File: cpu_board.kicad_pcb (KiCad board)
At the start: 4 copper layers, 63 parts, among them J1 Conn_01x13, J10 Conn_02x12_Odd_Even, J11 Conn_02x12_Odd_Even, J12 Conn_02x12_Odd_Even, J13 Conn_02x12_Odd_Even, J14 Conn_02x12_Odd_Even, J15 Conn_02x12_Odd_Even, J2 Conn_02x05_Odd_Even, J3 Conn_02x12_Odd_Even, J4 Conn_01x13, J5 Conn_02x12_Odd_Even, J6 Conn_02x12_Odd_Even, J7 Conn_02x12_Odd_Even, J8 Conn_02x12_Odd_Even, J9 Conn_02x12_Odd_Even, U1 74HC191, U2 74HC191, U3 74HC191, U4 74HC245, U5 74HC245, U6 74HC02, U7 74HC08

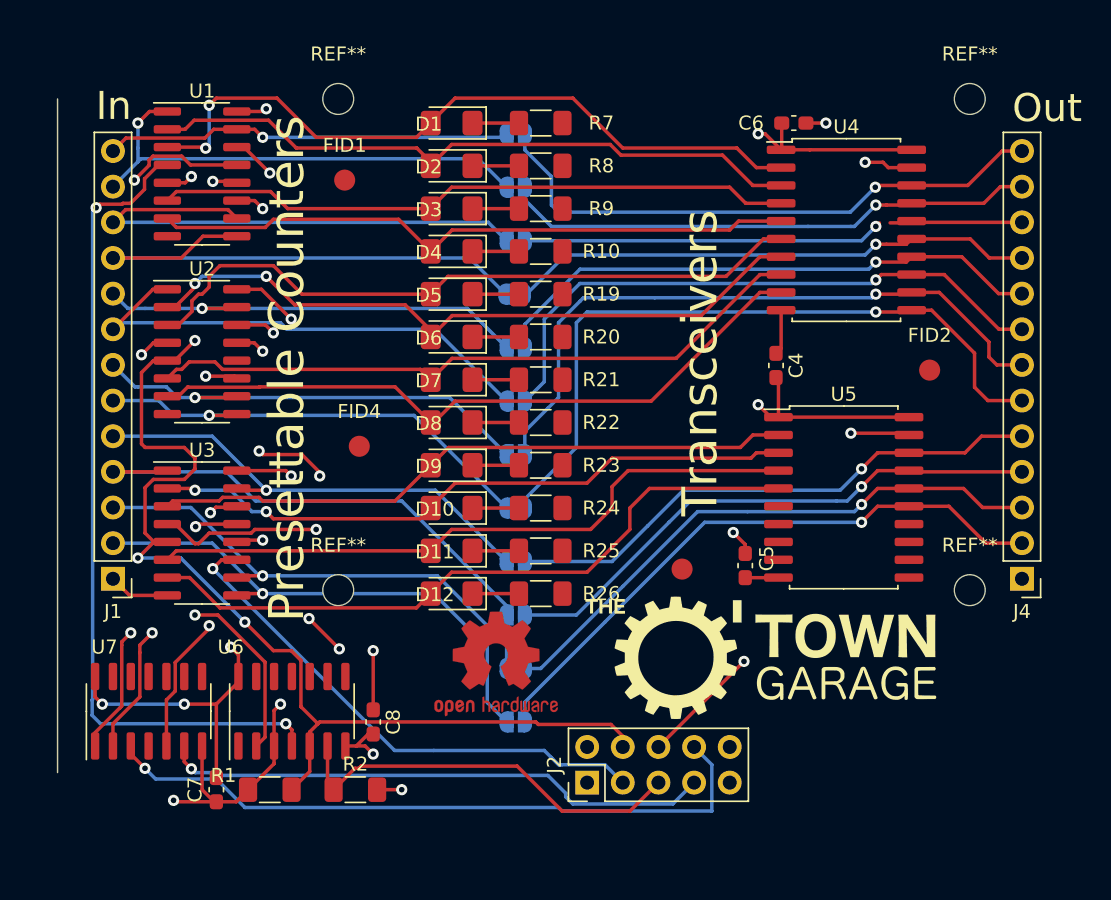
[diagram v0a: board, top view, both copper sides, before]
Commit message: Add edge cuts
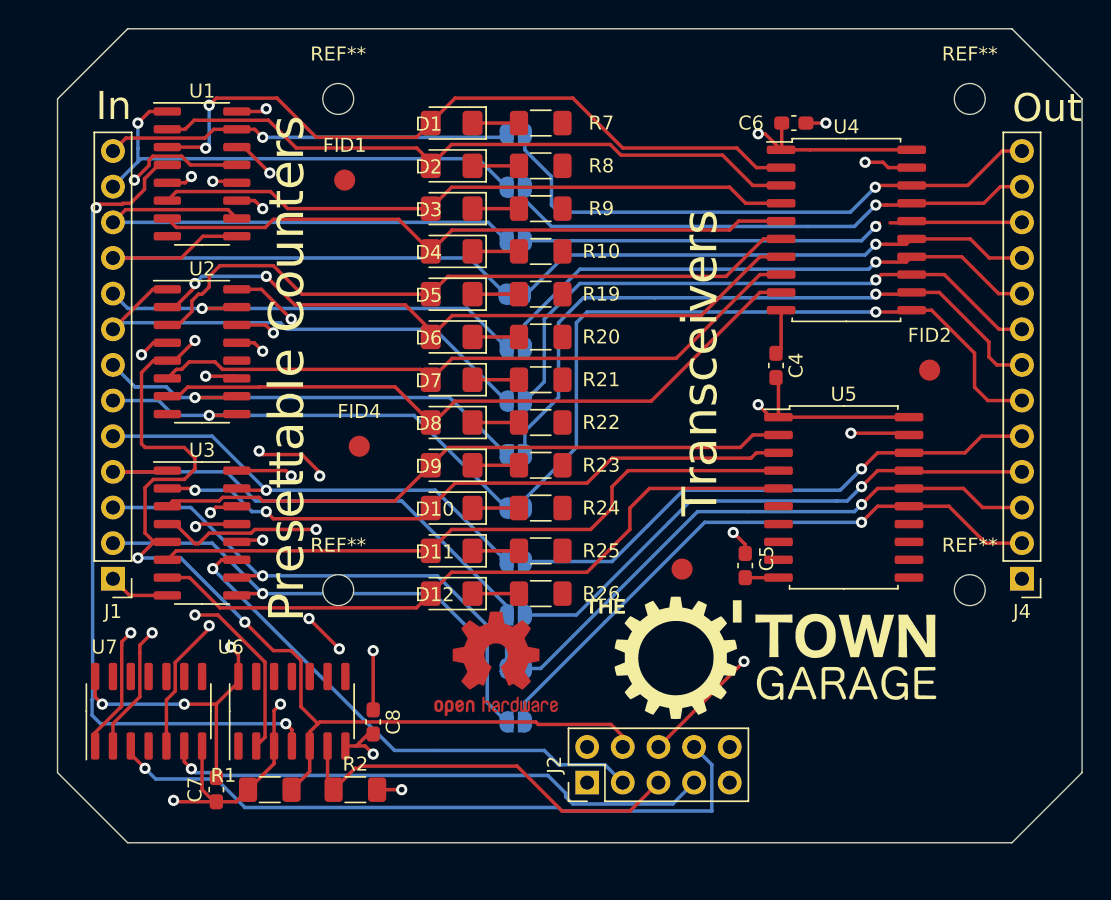
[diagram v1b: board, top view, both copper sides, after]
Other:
- board outline added: 73 x 58 mm
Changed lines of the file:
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@@
       ))
   )
+  (gr_line (start 123 103) (end 123 55) (layer "Edge.Cuts") (width 0.1))
+  (gr_line (start 118 50) (end 55 50) (layer "Edge.Cuts") (width 0.1))
+  (gr_line (start 123 55) (end 118 50) (layer "Edge.Cuts") (width 0.1))
+  (gr_line (start 118 108) (end 123 103) (layer "Edge.Cuts") (width 0.1))
+  (gr_line (start 55 50) (end 50 55) (layer "Edge.Cuts") (width 0.1))
   (gr_line (start 50 55) (end 50 103) (layer "Edge.Cuts") (width 0.1))
+  (gr_line (start 55 108) (end 118 108) (layer "Edge.Cuts") (width 0.1))
+  (gr_line (start 55 108) (end 50 103) (layer "Edge.Cuts") (width 0.1))
   (gr_text "Transceivers" (at 95.783 73.8134 90) (layer "F.SilkS")
     (effects (font (size 2.5 2.5) (thickness 0.4)))

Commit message: routed and pretty
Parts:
- removed the REF** at (81.2, 95.2)
- added C1: 100nF, Capacitor_SMD:C_0603_1608Metric_Pad1.08x0.95mm_HandSolder, F.Cu at (61.9, 54.3)
- added C2: 100nF, Capacitor_SMD:C_0603_1608Metric_Pad1.08x0.95mm_HandSolder, F.Cu at (60.5, 66.8)
- added C3: 100nF, Capacitor_SMD:C_0603_1608Metric_Pad1.08x0.95mm_HandSolder, F.Cu at (60.4, 79.4)
- moved REF** 22.7 mm to (53.0, 105.0)
- moved REF** 17.0 mm to (53.0, 55.0)
- moved REF** 15.3 mm to (118.0, 105.0)
- moved C7 14.6 mm to (52.0, 93.0)
- moved J2 8.50 mm to (79.2, 104.2), turned to 180 degrees
- moved ? 5.55 mm to (104.0, 98.6)
- moved REF** 3.00 mm to (118.0, 55.0)
- turned C8 to 90 degrees
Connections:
- J2 pad 2: CLK -> /Presettable counters/UNDERFLOW
- J2 pad 5: /Presettable counters/~{INC}/DEC -> /Presettable counters/~{TRANSC_ENA}
- J2 pad 6: /Presettable counters/~{TRANSC_ENA} -> /Presettable counters/~{INC}/DEC
- J2 pad 8: /Presettable counters/UNDERFLOW -> CLK
- U2 pad 15: unconnected-(U2-Pad15) -> /Presettable counters/IN_4
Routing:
- net GND: track 30.4 -> 74.1 mm, vias 4 -> 21
- net /Presettable counters/UNDERFLOW: track 48.8 -> 24.5 mm
- net /Presettable counters/INC/~{DEC}: track 88.3 -> 68.0 mm, vias 4 -> 5
- net /Presettable counters/~{INC}/DEC: track 29.3 -> 12.5 mm
- net /Presettable counters/~{TRANSC_ENA}: track 55.4 -> 71.7 mm, vias 3 -> 2
- net CLK: track 70.0 -> 56.8 mm, vias 5 -> 4
- net /Presettable counters/OVERFLOW: track 39.5 -> 26.8 mm, vias 1 -> 2
- net /Presettable counters/~{SET_CNT}: track 70.7 -> 59.2 mm
- net VCC: track 202.4 -> 193.3 mm, vias 11 -> 9
- net Net-(U6-Pad1): track 0.83 -> 8.67 mm, vias 0 -> 2
- net /Presettable counters/IN_3: track 38.5 -> 32.0 mm, vias 0 -> 1
- net /Presettable counters/CNT_0: track 51.3 -> 47.9 mm
- net /Presettable counters/~{RCO_2}: track 30.0 -> 32.4 mm
- net /Presettable counters/IN_9: track 36.6 -> 34.3 mm, vias 0 -> 1
- net /Presettable counters/CNT_4: track 48.9 -> 50.9 mm
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- added copper zone on In2.Cu, net GND
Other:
- board size 73 x 58 mm -> 75 x 60 mm
- board text added: "CLK"
- board text added: "DEC"
- board text added: "GND"
- board text added: "INC"
- board text added: "OVERFLOW"
- board text added: "UNDERFLOW"
- board text added: "VCC"
- board text added: "~{SET CNT}"
- board text added: "~{TRANSC ENA}"

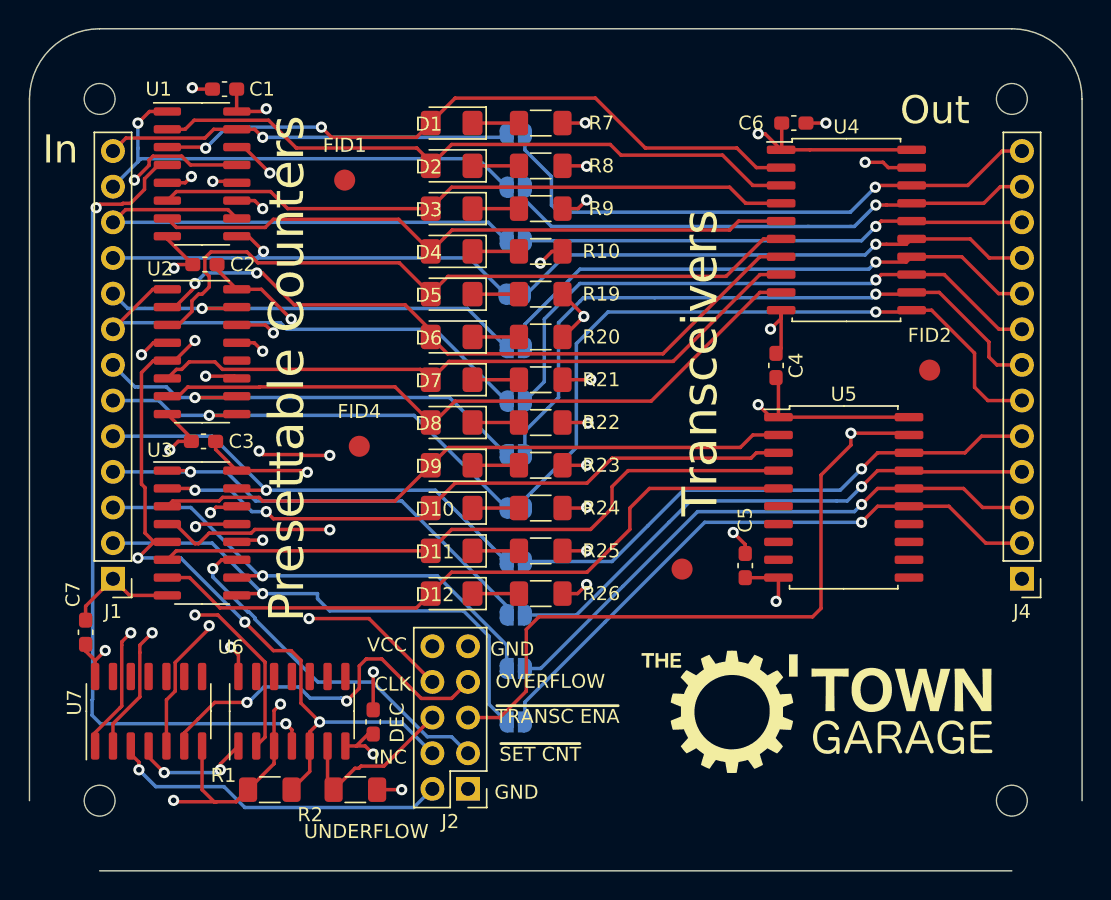
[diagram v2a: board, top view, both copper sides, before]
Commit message: Fixed DRC errors
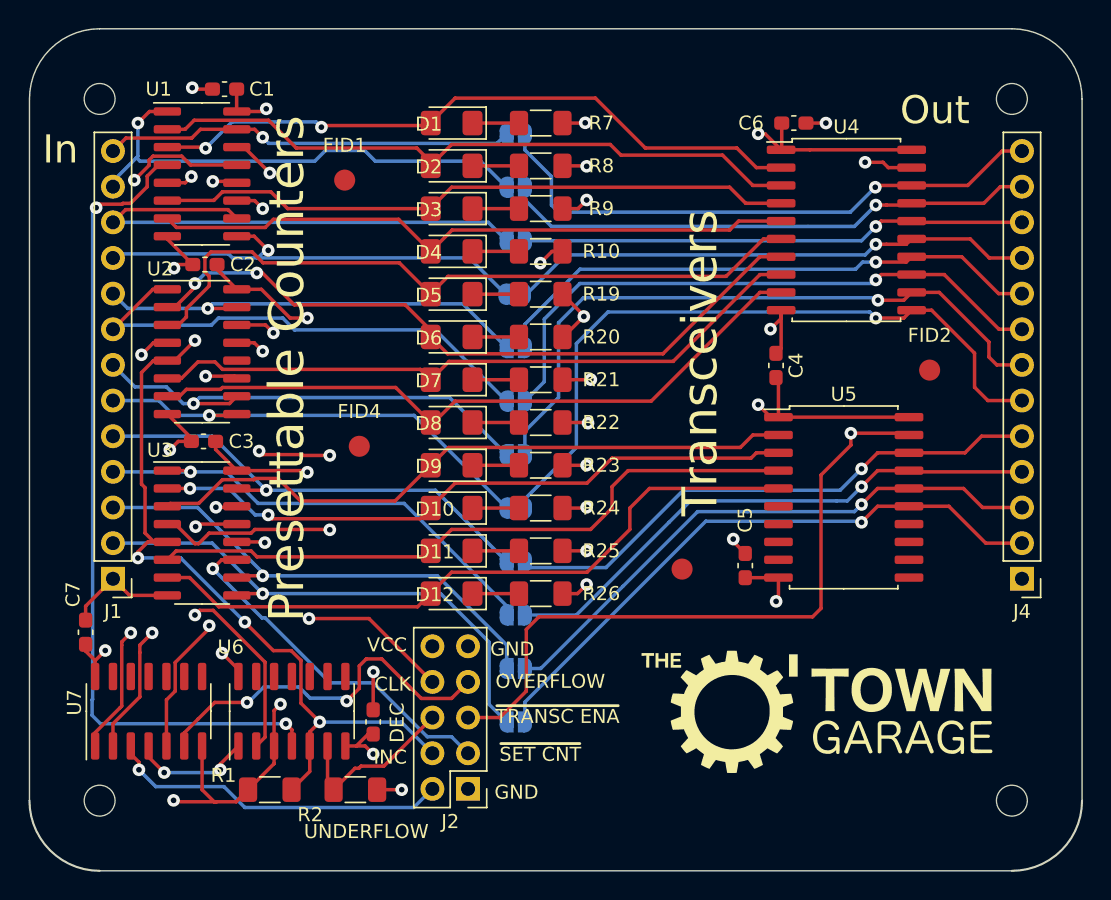
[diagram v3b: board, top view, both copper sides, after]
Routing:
- net /Presettable counters/INC/~{DEC}: track 68.0 -> 70.7 mm
- net /Presettable counters/CNT_8: track 45.9 -> 47.0 mm
- net /Presettable counters/IN_3: track 32.0 -> 32.9 mm
- net /Presettable counters/IN_1: track 34.9 -> 35.6 mm
- net /Presettable counters/IN_6: track 33.7 -> 34.4 mm
- net /Presettable counters/MAX/MIN_1: track 45.6 -> 46.2 mm
